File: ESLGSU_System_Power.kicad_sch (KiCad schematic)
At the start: 0 parts

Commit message: Started work on system power section
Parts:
- added C1, C8: 1n, Capacitor_SMD:C_0603_1608Metric, symbol Device:C_Small
- added C10, C11, C4, C5, C6: 100n, Capacitor_SMD:C_0603_1608Metric, symbol Device:C_Small
- added C2, C7: 1u, Capacitor_SMD:C_0603_1608Metric, symbol Device:C_Small
- added C3, C9: 22n, Capacitor_SMD:C_0603_1608Metric, symbol Device:C_Small
- added R1, R3: 10K, Resistor_SMD:R_0603_1608Metric, symbol Device:R_Small_US
- added R2: 5m, Resistor_SMD:R_0603_1608Metric, symbol Device:R_Small_US
- added U2, U6: DML3012LDC, Package_DFN_QFN:WDFN-12-1EP_3x3mm_P0.45mm_EP1.7x2.5mm, symbol ESLGSU_Parts_Lib:DML3012LDC-7
- added U3, U8: LM74700, Package_TO_SOT_SMD:SOT-23-6, symbol Power_Management:LM74700
- added U4, U7: ~, ESLGSU_Parts_Lib:V-DFN3030-8, symbol ESLGSU_Parts_Lib:DMT3006LDK
- added U5: INA219AxDCN, Package_TO_SOT_SMD:SOT-23-8, symbol Sensor_Energy:INA219AxDCN
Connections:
- net BUS_UNREG: now also R2.2, U5.2 (IN-)
- net EN_BAT_UNREG: now also U6.2 (EN)
- net EN_P_IN_UNREG: now also U2.2 (EN)
- net EPS_SCL: now also U5.5 (SCL)
- net EPS_SDA: now also U5.6 (SDA)
- net POWER_IN: now also U2.1 (VIN), U2.13 (VIN)
- new net: C10.1, U8.1 (VCAP)
- new net: U7.1 (G), U8.5 (GATE)
- new net: C9.1, U6.10 (VOUT), U6.11 (VOUT), U6.12 (VOUT), U6.8 (VOUT), U6.9 (VOUT), U7.2 (S), U8.6 (ANODE)
- new net: C11.1, C4.1, R2.1, U3.4 (CATHODE), U4.3 (D), U5.1 (IN+), U7.3 (D), U8.4 (CATHODE)
- new net: R3.2, U6.6 (PG), U8.3 (EN)
- new net: C2.1, R1.1, U2.3 (VCC)
- new net: R1.2, U2.6 (PG), U3.3 (EN)
- new net: C7.1, R3.1, U6.3 (VCC)
- new net: U3.5 (GATE), U4.1 (G)
- new net: C3.1, U2.10 (VOUT), U2.11 (VOUT), U2.12 (VOUT), U2.8 (VOUT), U2.9 (VOUT), U3.6 (ANODE), U4.2 (S)
- new net: C6.1, U5.4 (VS)
- new net: U6.1 (VIN), U6.13 (VIN)
- new net: C8.1, U6.5 (SR)
- new net: C1.1, U2.5 (SR)
- new net: C5.1, U3.1 (VCAP)
- new net GND: C6.2, U5.3 (GND), U5.7 (A0), U5.8 (A1)
- new net GNDA: C1.2, C10.2, C11.2, C2.2, C3.2, C4.2, C5.2, C7.2, C8.2, C9.2, U2.4 (GND), U3.2 (GND), U6.4 (GND), U8.2 (GND)
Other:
- note added: "15A max, 20V max RDSon 4.8-6.1mOhm Prot: UVLO, short, current, thermal"
- note added: "ADD 3V3"
- note added: "ADD 5V"
- note added: "Adr: 1000000"
- note added: "Ideal Diode"
- note added: "Load Switch"
- note added: "Power Monitoring"

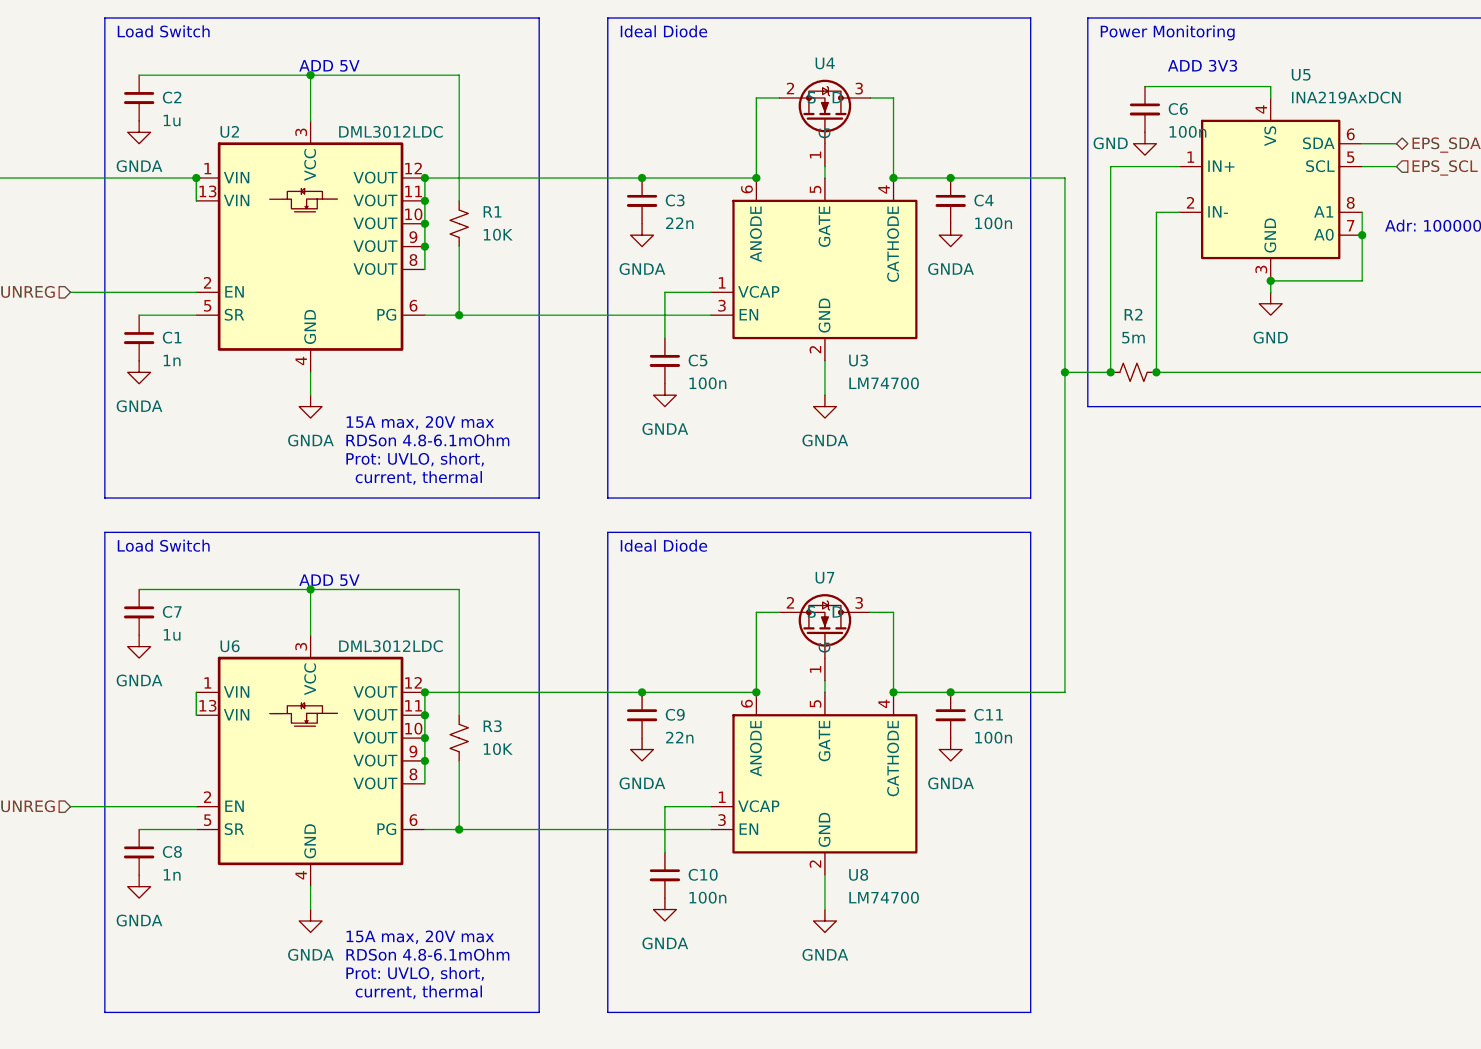
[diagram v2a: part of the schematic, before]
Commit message: Additional power regulation work
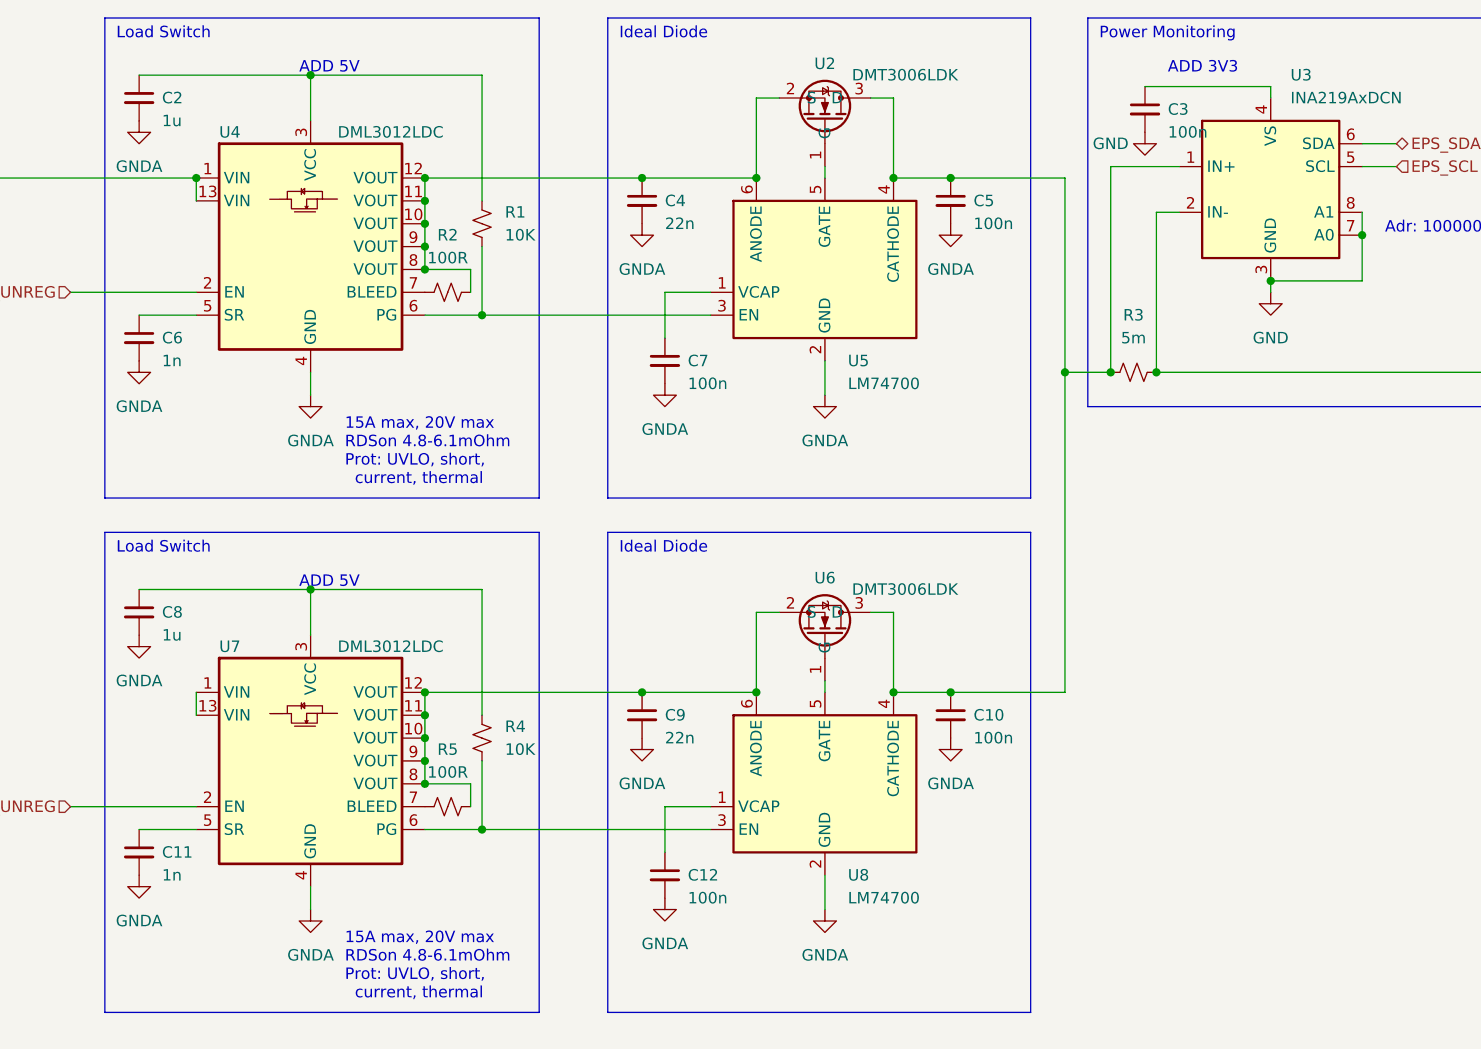
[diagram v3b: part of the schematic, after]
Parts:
- added R2, R5: 100R, Resistor_SMD:R_0603_1608Metric, symbol Device:R_Small_US
- U2: renamed from U4; value ~ -> DMT3006LDK
- U6: renamed from U7; value ~ -> DMT3006LDK
- renumbered C11 to C10, C8 to C11, C10 to C12, C6 to C3, C3 to C4, C4 to C5, C1 to C6, C5 to C7, C7 to C8, R2 to R3, R3 to R4, U5 to U3, U2 to U4, U3 to U5, U6 to U7
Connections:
- net at C9.1, U6.2 (S), U7.10 (VOUT)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: now also R5.2
- net at C4.1, U2.2 (S), U4.10 (VOUT)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: now also R2.2
- new net: R5.1, U7.7 (BLEED)
- new net: R2.1, U4.7 (BLEED)
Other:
- moved on the sheet: R1, R4

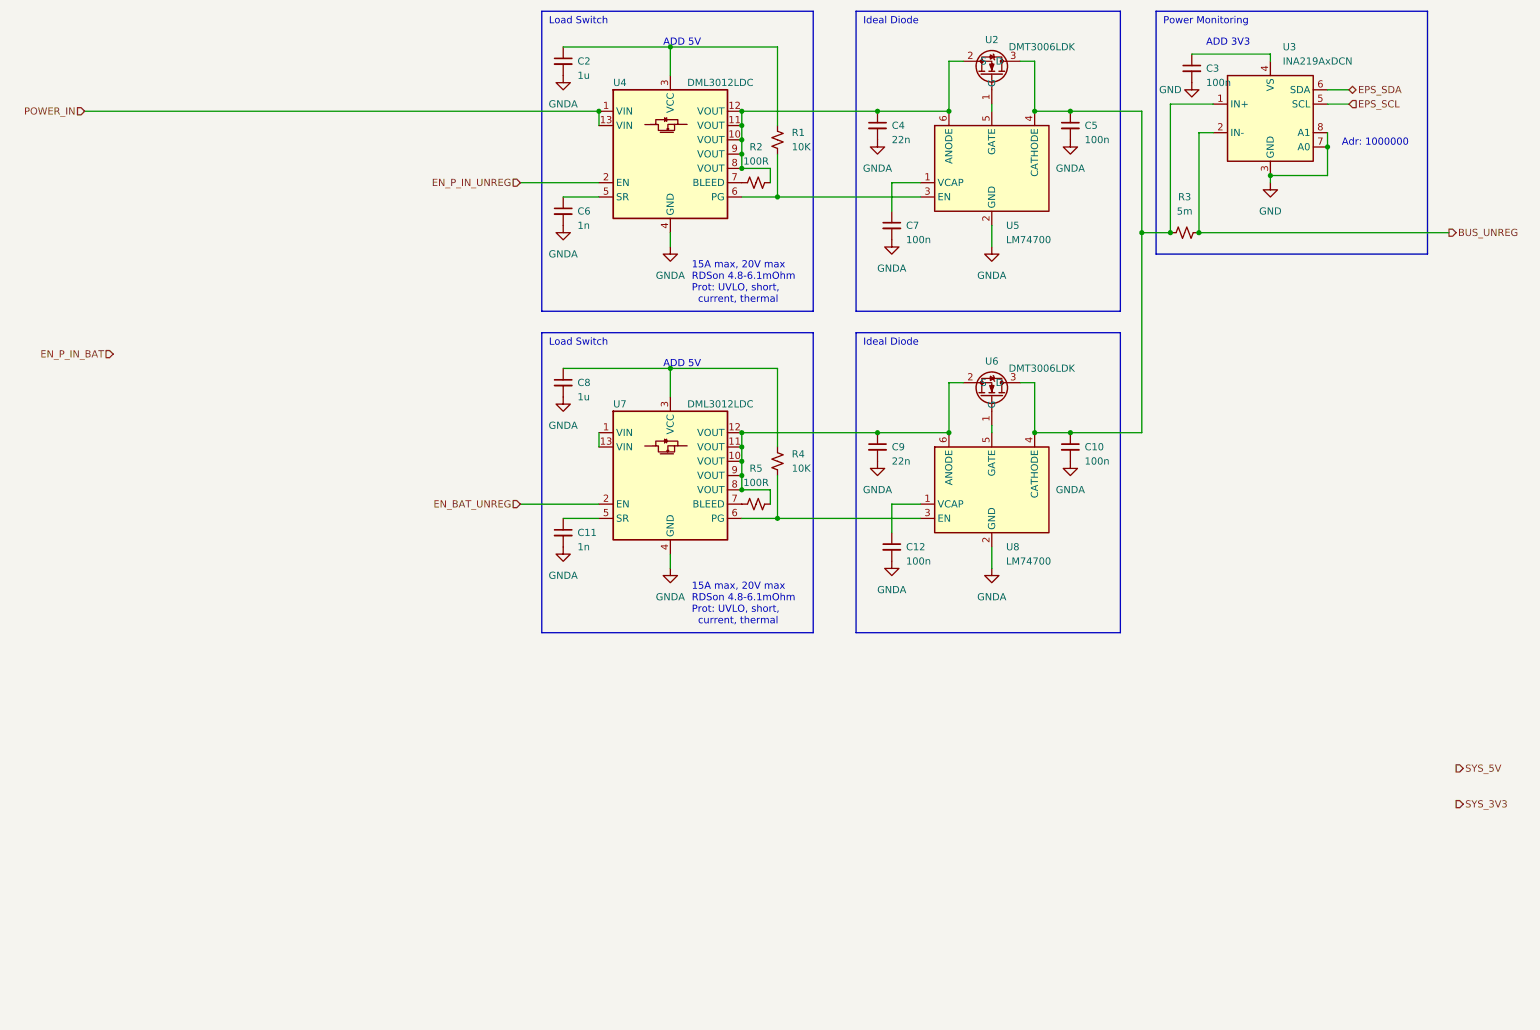
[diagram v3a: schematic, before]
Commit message: Added 5v/3V3 regulators and mux
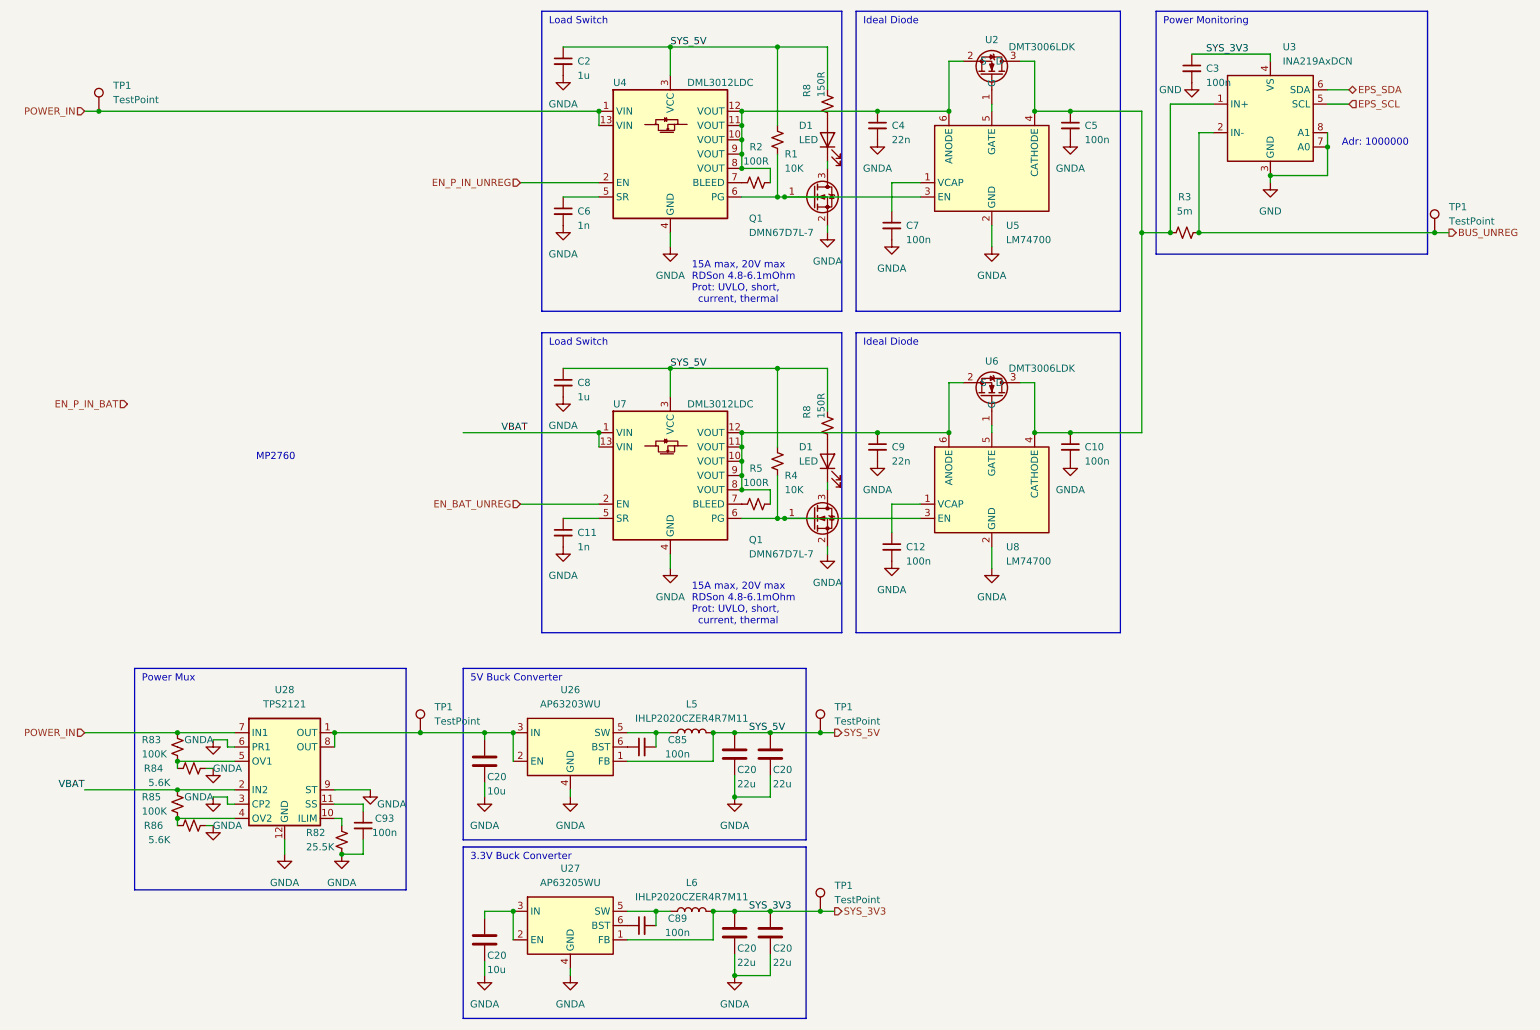
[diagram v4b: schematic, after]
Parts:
- added C20 (x4): 22u, Capacitor_SMD:C_0805_2012Metric, symbol Device:C
- added C20 (x2): 10u, Capacitor_SMD:C_0805_2012Metric, symbol Device:C
- added C85, C89, C93: 100n, Capacitor_SMD:C_0603_1608Metric, symbol Device:C_Small
- added D1 (x2): LED, LED_SMD:LED_0603_1608Metric, symbol Device:LED
- added L5, L6: IHLP2020CZER4R7M11, Inductor_SMD:L_Vishay_IHLP-2020, symbol Device:L
- added Q1 (x2): DMN67D7L-7, Package_TO_SOT_SMD:SOT-323_SC-70, symbol Transistor_FET:DMN67D7L
- added R8 (x2): 150R, Resistor_SMD:R_0603_1608Metric, symbol Device:R_Small_US
- added R82: 25.5K, Resistor_SMD:R_0603_1608Metric, symbol Device:R_Small_US
- added R83, R85: 100K, Resistor_SMD:R_0603_1608Metric, symbol Device:R_Small_US
- added R84, R86: 5.6K, Resistor_SMD:R_0603_1608Metric, symbol Device:R_Small_US
- added TP1 (x5): TestPoint, TestPoint:TestPoint_Pad_D2.0mm, symbol Connector:TestPoint
- added U26: AP63203WU, Package_TO_SOT_SMD:TSOT-23-6, symbol Regulator_Switching:AP63203WU
- added U27: AP63205WU, Package_TO_SOT_SMD:TSOT-23-6, symbol Regulator_Switching:AP63205WU
- added U28: TPS2121, Package_DFN_QFN:Texas_VQFN-HR-12_2x2.5mm_P0.5mm_ThermalVias, symbol ESLGSU_Parts_Lib:TPS2121
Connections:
- net BUS_UNREG: now also TP1.1
- net GNDA: now also C20.2, C20.2, C20.2, C20.2, C20.2, C20.2, C93.2, Q1.2 (S), Q1.2 (S), R82.1, R84.1, R86.1, U26.4 (GND), U27.4 (GND), U28.12 (GND), U28.3 (CP2), U28.6 (PR1), U28.9 (ST)
- net POWER_IN: now also R83.2, TP1.1, U28.7 (IN1)
- net SYS_3V3: now also C3.1, U3.4 (VS), C20.1, C20.1, L6.2, TP1.1, U27.1 (FB)
- net SYS_5V: now also C2.1, C8.1, R1.1, R4.1, U4.3 (VCC), U7.3 (VCC), C20.1, C20.1, L5.2, R8.1, R8.1, TP1.1, U26.1 (FB)
- net at R4.2, U7.6 (PG), U8.3 (EN): now also Q1.1 (G)
- net at R1.2, U4.6 (PG), U5.3 (EN): now also Q1.1 (G)
- net VBAT: now reaches U7.1 (VIN), U7.13 (VIN)
- net VBAT: now also R85.2, U28.2 (IN2)
- new net: R85.1, R86.2, U28.4 (OV2)
- new net: C85.1, U26.6 (BST)
- new net: C85.2, L5.1, U26.5 (SW)
- new net: C20.1, U27.2 (EN), U27.3 (IN)
- new net: C20.1, TP1.1, U26.2 (EN), U26.3 (IN), U28.1 (OUT), U28.8 (OUT)
- new net: R82.2, U28.10 (ILIM)
- new net: C93.1, U28.11 (SS)
- new net: R83.1, R84.2, U28.5 (OV1)
- new net: C89.1, U27.6 (BST)
- new net: C89.2, L6.1, U27.5 (SW)
- new net: D1.1 (K), Q1.3 (D) (x2)
- new net: D1.2 (A), R8.2 (x2)
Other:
- note added: "3.3V Buck Converter"
- note added: "5V Buck Converter"
- note added: "MP2760"
- note added: "Power Mux"
- note removed: "ADD 3V3"
- note removed: "ADD 5V"

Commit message: uC Interface work
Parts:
- Q1: footprint Package_TO_SOT_SMD:SOT-323_SC-70 -> Package_TO_SOT_SMD:SOT-23
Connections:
- net SYS_3V3: now also U26.1 (FB); no longer U27.1 (FB)
- net SYS_5V: now also U27.1 (FB); no longer U26.1 (FB)
- net at C85.1: now also U27.6 (BST); no longer U26.6 (BST)
- net at C85.2, L5.1: now also U27.5 (SW); no longer U26.5 (SW)
- net at C20.1, U27.2 (EN), U27.3 (IN): now also C20.1, TP1.1, U26.2 (EN), U26.3 (IN), U28.1 (OUT), U28.8 (OUT)
- net at C89.1: now also U26.6 (BST); no longer U27.6 (BST)
- net at C89.2, L6.1: now also U26.5 (SW); no longer U27.5 (SW)
